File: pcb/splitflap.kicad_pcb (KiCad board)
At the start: 2 copper layers, 96 x 45 mm, 62 parts, among them J1 Motor A, J10 Hall C, J11 Hall-D, J12 Conn_01x03, J13 Conn_01x03, J14 Conn_01x03, J15 Conn_01x03, J2 Motor B, J3 Motor C, J4 Motor D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

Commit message: Make sure mouse bites aren't deleted upon import
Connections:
- J7 pad 1: +5V -> +12V
- J7 pad 3: unconnected-(J7-Pad3) -> GND
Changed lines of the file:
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@@
   (net 63 "Net-(J6-Pin_1)")
   (net 64 "Net-(J6-Pin_3)")
-  (net 65 "unconnected-(J7-Pad3)")
+  (net 65 "+12V")
   (net 66 "Net-(J12-Pin_3)")
   (net 67 "Net-(J12-Pin_2)")
@@
       (stroke (width 0.1) (type solid)) (layer "F.Fab"))
     (pad "1" thru_hole rect (at 0 0 90) (size 4.6 2) (drill oval 3.6 1) (layers "*.Cu" "*.Mask")
-      (net 8 "+5V") (pintype "passive"))
+      (net 65 "+12V") (pintype "passive"))
     (pad "2" thru_hole oval (at 0 6.3 90) (size 4.2 2) (drill oval 3.2 1) (layers "*.Cu" "*.Mask")
       (net 29 "GND") (pintype "passive"))
     (pad "3" thru_hole oval (at 4.8 2.9 90) (size 2 4.2) (drill oval 1 3.2) (layers "*.Cu" "*.Mask")
-      (net 65 "unconnected-(J7-Pad3)") (pintype "passive+no_connect"))
+      (net 29 "GND") (pintype "passive"))
     (model "${KICAD6_3DMODEL_DIR}/Connector_BarrelJack.3dshapes/BarrelJack_GCT_DCJ200-10-A_Horizontal.wrl"
       (offset (xyz 0 0 0))
@@
   (footprint "Panelization:mouse-bite-2mm-slot" (layer "F.Cu")
     (at 166 117.5 90)
-    (attr through_hole)
+    (attr through_hole board_only)
     (fp_text reference "mouse-bite-2mm-slot1" (at 0 -2 90) (layer "F.SilkS") hide
         (effects (font (size 1 1) (thickness 0.2)))
@@
   (footprint "Panelization:mouse-bite-2mm-slot" (layer "F.Cu")
     (at 166 108.5 90)
-    (attr through_hole)
+    (attr through_hole board_only)
     (fp_text reference "mouse-bite-2mm-slot3" (at 0 -2 90) (layer "F.SilkS") hide
         (effects (font (size 1 1) (thickness 0.2)))
@@
   (footprint "Panelization:mouse-bite-2mm-slot" (layer "F.Cu")
     (at 166 126.5 90)
-    (attr through_hole)
+    (attr through_hole board_only)
     (fp_text reference "mouse-bite-2mm-slot" (at 0 -2 90) (layer "F.SilkS") hide
         (effects (font (size 1 1) (thickness 0.2)))
@@
   (footprint "Panelization:mouse-bite-2mm-slot" (layer "F.Cu")
     (at 166 99.5 90)
-    (attr through_hole)
+    (attr through_hole board_only)
     (fp_text reference "mouse-bite-2mm-slot5" (at 0 -2 90) (layer "F.SilkS") hide
         (effects (font (size 1 1) (thickness 0.2)))
@@
   (footprint "Panelization:mouse-bite-2mm-slot" (layer "F.Cu")
     (at 176.5 113 180)
-    (attr through_hole)
+    (attr through_hole board_only)
     (fp_text reference "mouse-bite-2mm-slot2" (at 0 -2) (layer "F.SilkS") hide
         (effects (font (size 1 1) (thickness 0.2)))
@@
   (footprint "Panelization:mouse-bite-2mm-slot" (layer "F.Cu")
     (at 166 90.5 90)
-    (attr through_hole)
+    (attr through_hole board_only)
     (fp_text reference "mouse-bite-2mm-slot7" (at 0 -2 90) (layer "F.SilkS") hide
         (effects (font (size 1 1) (thickness 0.2)))
@@
   (footprint "Panelization:mouse-bite-2mm-slot" (layer "F.Cu")
     (at 176.5 122 180)
-    (attr through_hole)
+    (attr through_hole board_only)
     (fp_text reference "mouse-bite-2mm-slot" (at 0 -2) (layer "F.SilkS") hide
         (effects (font (size 1 1) (thickness 0.2)))
@@
   (footprint "Panelization:mouse-bite-2mm-slot" (layer "F.Cu")
     (at 176.5 104 180)
-    (attr through_hole)
+    (attr through_hole board_only)
     (fp_text reference "mouse-bite-2mm-slot4" (at 0 -2) (layer "F.SilkS") hide
         (effects (font (size 1 1) (thickness 0.2)))
@@
   (footprint "Panelization:mouse-bite-2mm-slot" (layer "F.Cu")
     (at 176.5 95 180)
-    (attr through_hole)
+    (attr through_hole board_only)
     (fp_text reference "mouse-bite-2mm-slot6" (at 0 -2) (layer "F.SilkS") hide
         (effects (font (size 1 1) (thickness 0.2)))

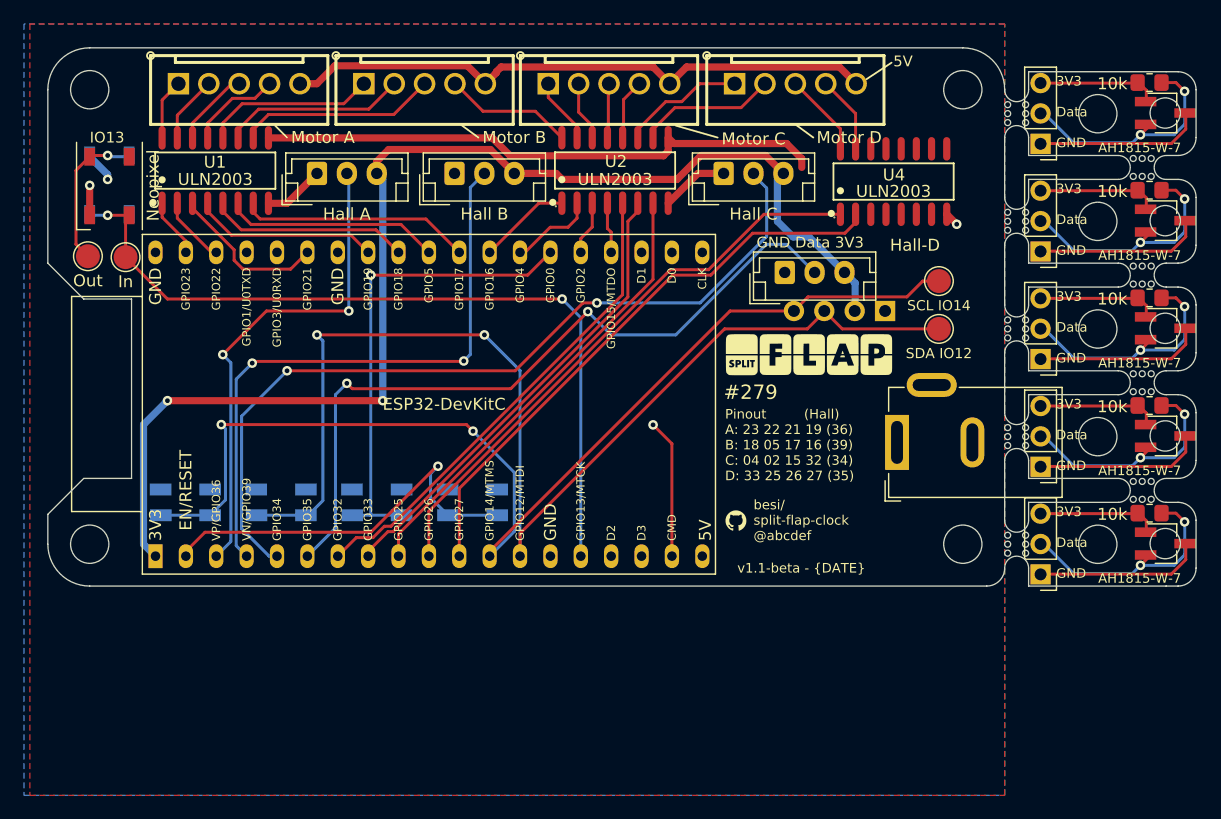
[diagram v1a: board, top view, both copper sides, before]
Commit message: Add 12V-enabled power supply
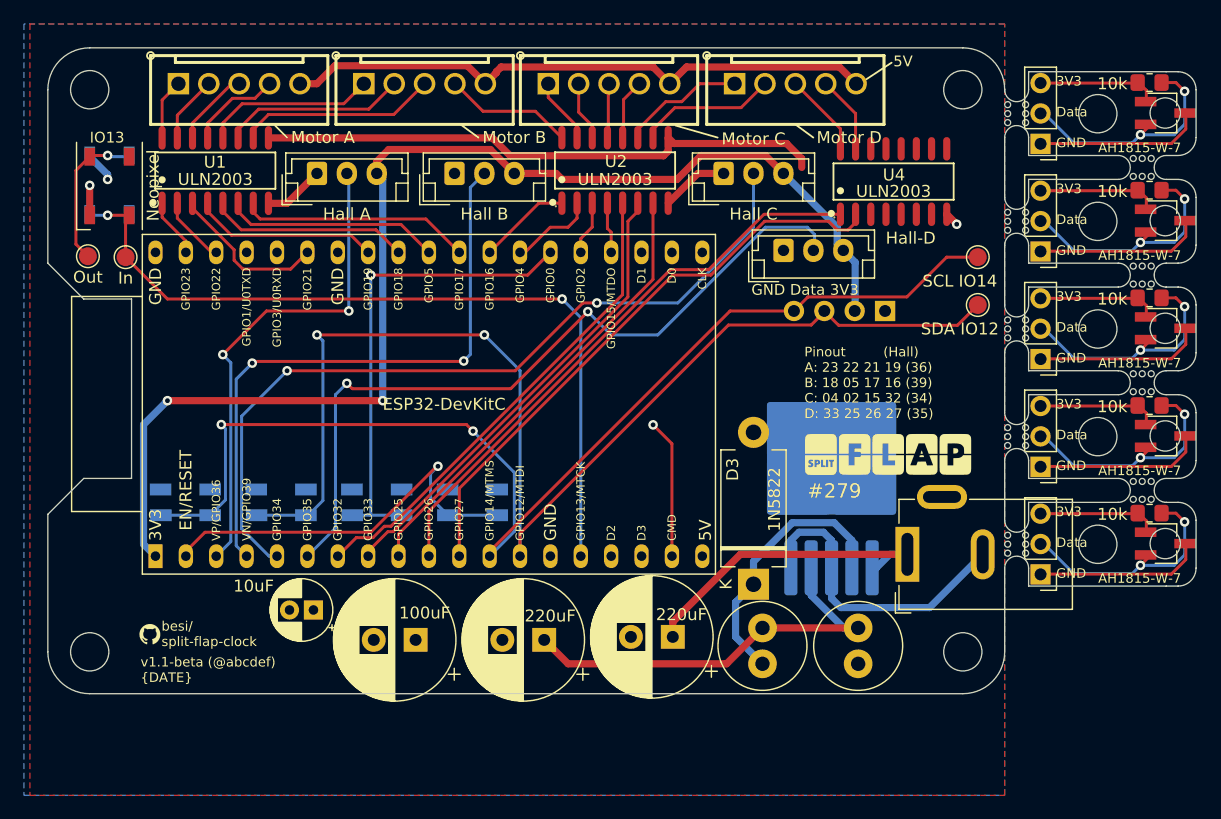
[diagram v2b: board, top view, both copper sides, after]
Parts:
- added C6: 220uF, Capacitor_THT:CP_Radial_D10.0mm_P3.50mm, F.Cu at (137.2, 134.2)
- added C7: 220uF, Capacitor_THT:CP_Radial_D10.0mm_P3.50mm, F.Cu at (126.5, 134.5)
- added C8: 100uF, Capacitor_THT:CP_Radial_D10.0mm_P3.50mm, F.Cu at (115.8, 134.5)
- added C9: 10uF, Capacitor_THT:CP_Radial_D5.0mm_P2.00mm, F.Cu at (107.2, 132.0)
- added D3: 1N5822, Diode_THT:D_DO-201_P12.70mm_Horizontal, F.Cu at (144.0, 129.8)
- added L1: 33uH, Inductor_THT:L_Radial_D7.2mm_P3.00mm_Murata_1700, F.Cu at (144.8, 136.5)
- added L2: 22uH, Inductor_THT:L_Radial_D7.2mm_P3.00mm_Murata_1700, F.Cu at (152.8, 133.5)
- added U12: LM2596S-5, Package_TO_SOT_SMD:TO-263-5_TabPin3, B.Cu at (150.5, 120.8)
- TP1, TP2, TP3, TP4: footprint TestPoint:TestPoint_Pad_D2.0mm -> TestPoint:TestPoint_Pad_D1.5mm
- moved G*** 49.9 mm to (93.5, 134.0)
- moved OSHW1 20.6 mm to (154.2, 95.5)
- moved G*** 18.0 mm to (108.8, 113.2)
- moved G*** 15.5 mm to (133.0, 117.5)
- moved G*** 10.6 mm to (155.2, 119.0)
- moved J7 9.40 mm to (156.9, 127.3)
- moved H2 9.00 mm to (88.5, 135.5)
- moved H4 9.00 mm to (161.5, 135.5)
- moved TP3 3.82 mm to (162.8, 106.5)
- moved TP4 3.82 mm to (162.8, 102.5)
- moved J11 1.84 mm to (146.5, 101.9)
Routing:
- net /POW_FB: track 0.00 -> 35.7 mm
- net +12V: track 0.00 -> 26.6 mm
- net GND: track 14.4 -> 40.3 mm
- net /POW_OUT: track 0.00 -> 22.6 mm
- net GPIO14: track 93.7 -> 97.8 mm
- net GPIO12: track 99.1 -> 103.0 mm
- net GPI34: track 69.2 -> 67.2 mm
- net GPI35: track 62.7 -> 63.9 mm
- net +3V3: track 104.5 -> 103.4 mm
- net GPIO27: track 48.7 -> 49.3 mm
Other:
- board size 96 x 45 mm -> 96 x 54 mm
- board text added: "besi/ split-flap-clock"
- board text added: "v1.1-beta (@abcdef) {DATE}"
- board text removed: "besi/ split-flap-clock @abcdef"
- board text removed: "v1.1-beta - {DATE}"

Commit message: Add qwiic adapter
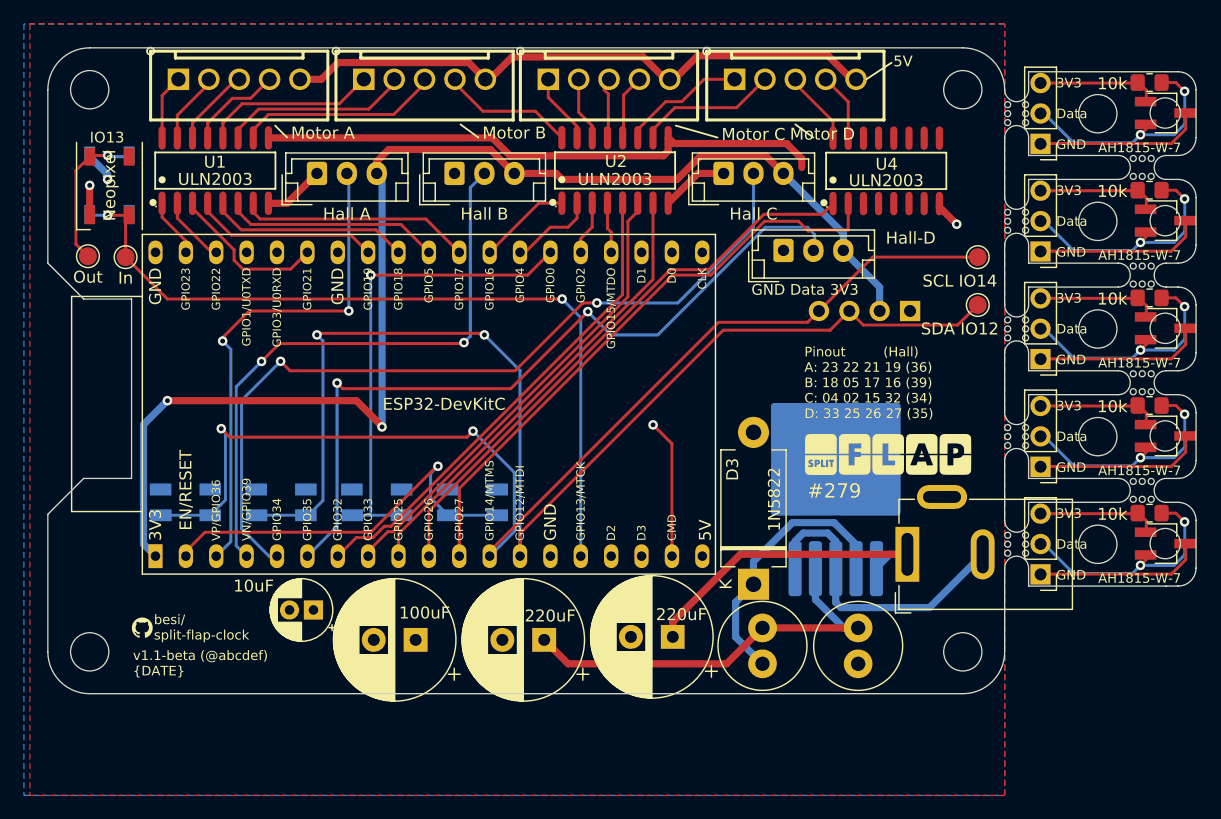
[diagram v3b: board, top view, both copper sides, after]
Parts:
- removed J5: I2C, Connector_PinHeader_2.54mm:PinHeader_1x04_P2.54mm_Vertical
- added U10: ~, qwiic-adapter:qwiic-adapter, B.Cu at (153.3, 107.0)
- moved U4 1.09 mm to (155.1, 95.3)
- moved G*** 0.84 mm to (92.9, 133.5)
- moved J1 0.37 mm to (101.0, 87.6)
- moved J2 0.37 mm to (116.5, 87.6)
- moved J3 0.37 mm to (131.9, 87.6)
- moved J4 0.37 mm to (147.5, 87.6)
- moved U12 0.36 mm to (150.9, 120.9)
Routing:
- net +3V3: track 103.4 -> 107.2 mm
- net GPI34: track 67.2 -> 68.6 mm
- net GPI39: track 51.2 -> 49.9 mm
- net GND: track 40.3 -> 41.3 mm
- net GPI36: track 41.3 -> 42.1 mm
- net Net-(U4-O1): track 7.00 -> 6.22 mm
- net Net-(U4-O2): track 6.48 -> 5.70 mm
- net +5V: track 100.6 -> 101.3 mm
- net GPIO27: track 49.3 -> 50.0 mm
- net GPI35: track 63.9 -> 64.5 mm
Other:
- board text added: "Pinout (Hall) A: 23 22 21 19 (36) B: 18 05 17 16 (39) C: 04 02 15 32 (34) D: 33 25 26 27 (35) Button A / SCL : 14 Button B / SDA : 12"

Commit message: Version 1.1-beta
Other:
- board text added: "v1.1 @f5de51 4. February 2025"
- board text removed: "v1.1-beta (@abcdef) {DATE}"
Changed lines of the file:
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@@
     (effects (font (size 0.9 0.9) (thickness 0.1)) (justify left))
   )
-  (gr_text "v1.1-beta (@abcdef)\n{DATE}\n" (at 92.114438 136.456581) (layer "F.SilkS")
+  (gr_text "v1.1 @f5de51\n4. February 2025" (at 92.114438 136.456581) (layer "F.SilkS")
     (effects (font (size 0.8 0.8) (thickness 0.1)) (justify left))
   )

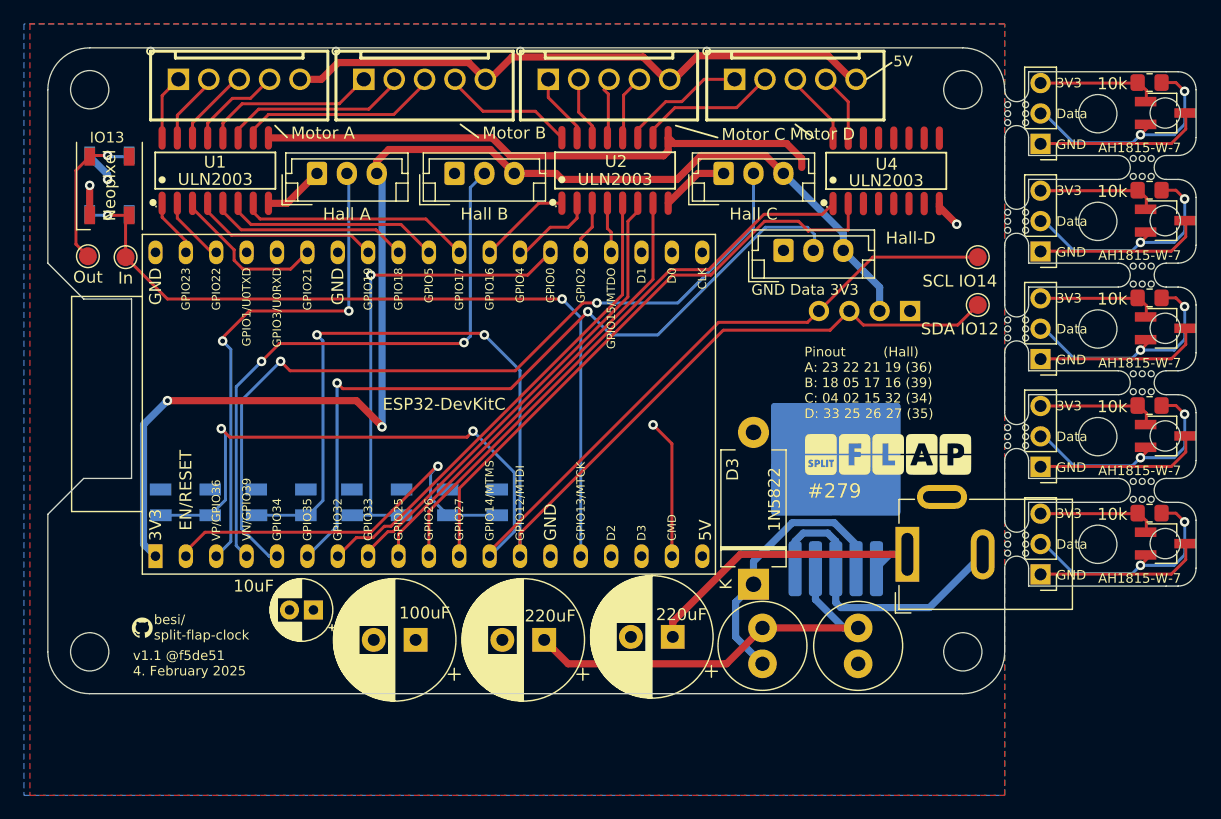
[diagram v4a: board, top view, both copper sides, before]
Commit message: Rework 1
Per EE.SO answer https://electronics.stackexchange.com/a/740530/10810
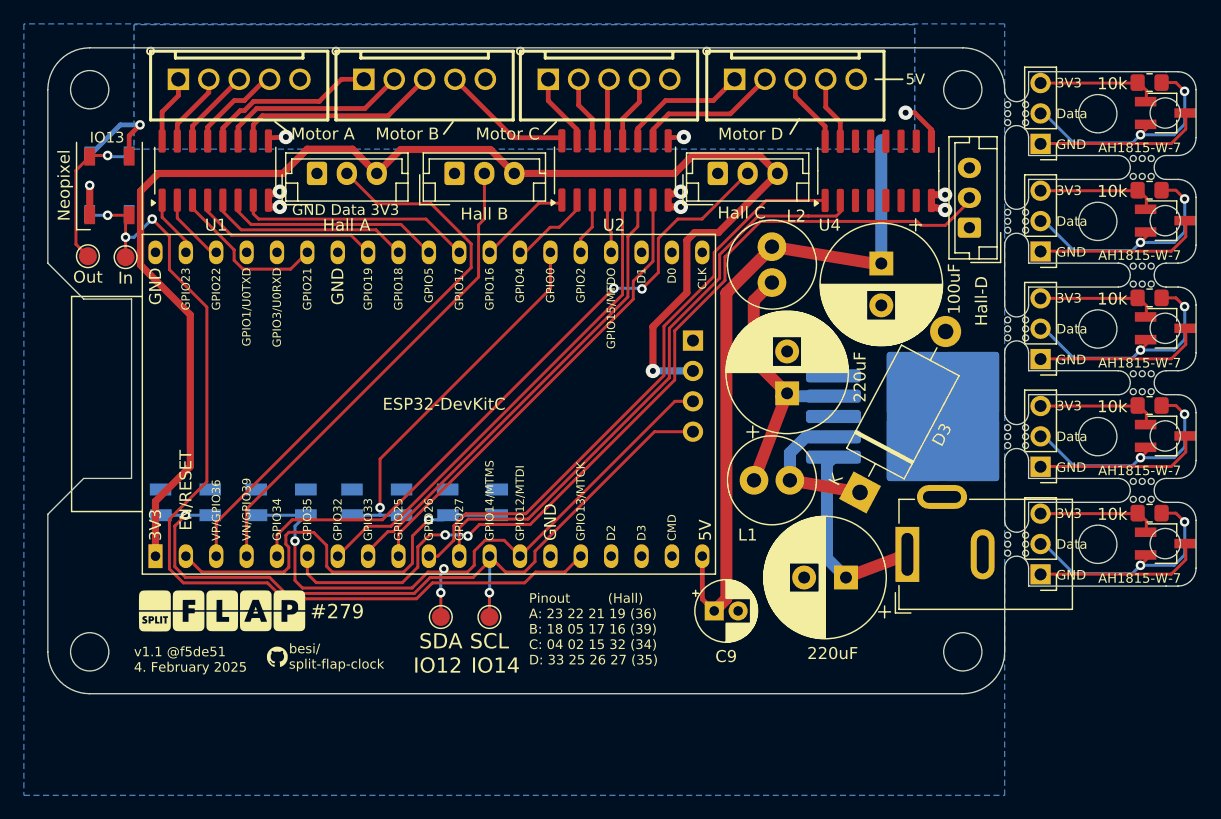
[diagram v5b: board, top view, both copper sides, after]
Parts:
- D3: footprint Diode_THT:D_DO-201_P12.70mm_Horizontal -> Diode_THT:D_DO-201_P15.24mm_Horizontal
- U1, U2, U4: footprint jlc_footprints:SOIC-16_L9.9-W3.9-P1.27-LS6.0-BL -> Package_SO:SOIC-16_3.9x9.9mm_P1.27mm
- moved G*** 57.2 mm to (99.6, 132.1)
- moved TP3 51.9 mm to (117.9, 132.6)
- moved TP4 50.7 mm to (121.9, 132.6)
- moved C8 50.1 mm to (154.7, 103.0), turned to -90 degrees
- moved OSHW1 45.3 mm to (130.6, 134.1)
- moved C9 33.5 mm to (140.7, 132.1), turned to 0 degrees
- moved L2 29.8 mm to (145.5, 104.6), turned to 90 degrees
- moved C7 28.9 mm to (146.8, 113.9), turned to 90 degrees
- moved J11 15.7 mm to (162.1, 100.0), turned to 90 degrees
- moved U10 15.7 mm to (138.9, 113.3), turned to 0 degrees
- moved L1 15.5 mm to (147.0, 121.2), turned to 180 degrees
- moved C6 15.3 mm to (151.7, 129.3)
- moved D3 11.8 mm to (152.9, 122.2), turned to 62 degrees
- moved G*** 11.6 mm to (104.2, 135.9)
- moved G*** 9.11 mm to (125.7, 112.0)
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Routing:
- net GPIO12: track 103.0 -> 56.1 mm, vias 2 -> 3
- net GND: track 41.3 -> 8.43 mm, vias 2 -> 7
- net GPIO14: track 97.7 -> 65.6 mm
- net +5V: track 101.3 -> 73.5 mm, vias 1 -> 4
- net GPI34: track 68.6 -> 55.4 mm
- net /POW_FB: track 35.5 -> 22.8 mm
- net GPIO13: track 67.1 -> 79.2 mm, vias 2 -> 3
- net unconnected-(U3-CMD-Pad18): track 11.6 -> 0.00 mm, vias 1 -> 0
- net GPI35: track 64.5 -> 75.5 mm
- net /POW_OUT: track 22.8 -> 12.4 mm
- net +3V3: track 107.2 -> 117.2 mm, vias 2 -> 1
- net +12V: track 26.3 -> 16.6 mm
- net GPI39: track 49.9 -> 40.2 mm, vias 2 -> 0
- net GPIO0: track 40.0 -> 32.0 mm
- net GPI36: track 42.1 -> 47.8 mm, vias 2 -> 0
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- added copper zone on B.Cu, net +5V
- removed copper zone on F.Cu, net +5V
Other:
- board text added: "GND 3V3 SDA SCL"
- board text removed: "Pinout (Hall) A: 23 22 21 19 (36) B: 18 05 17 16 (39) C: 04 02 15 32 (34) D: 33 25 26 27 (35) Button A / SCL : 14 Button B / SDA : 12"
- board text removed: "SCL SDA 3V3 GND"

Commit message: Rework 2
To be conservative, the traces driving the ULN2003s have been separated out, to prevent capacitive coupling between them. It's "cargo cult engineering", but since we can do it without trouble, how about we do it.
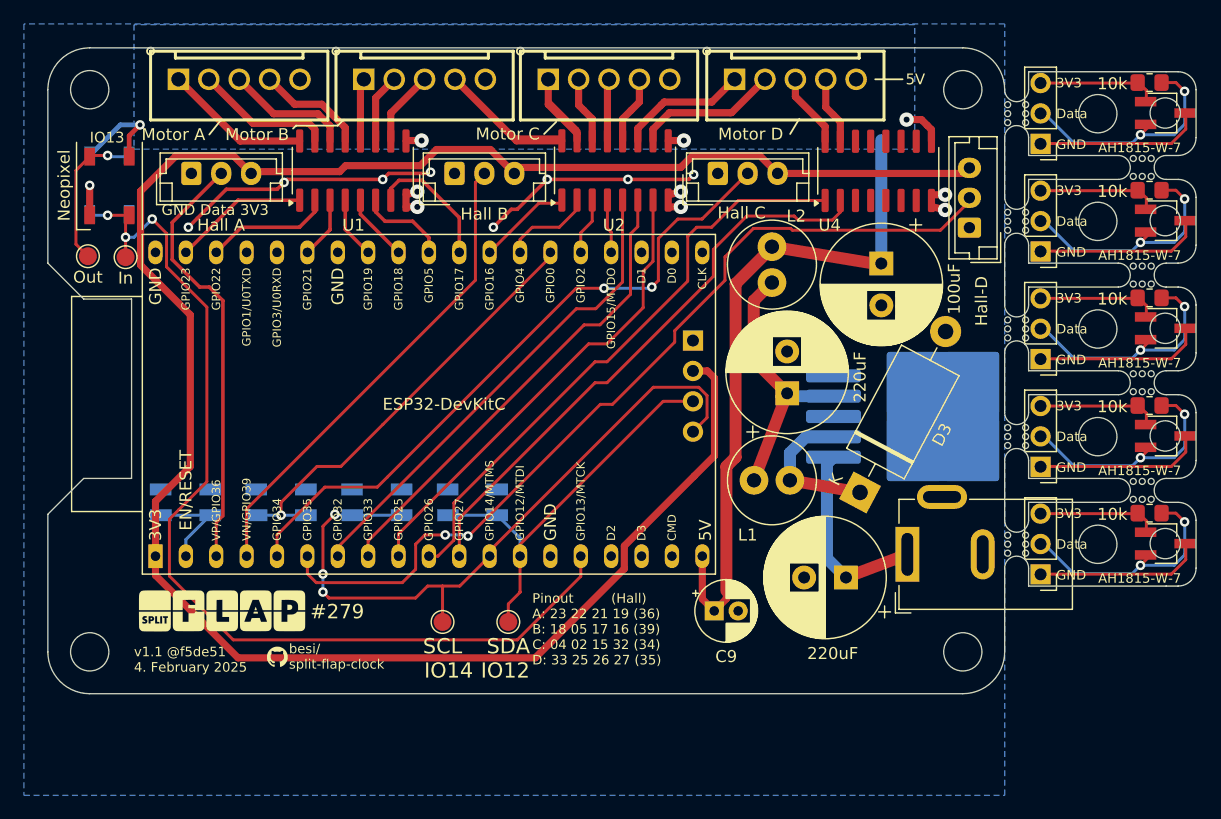
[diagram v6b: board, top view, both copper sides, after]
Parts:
- moved SW4 24.0 mm to (96.5, 123.0)
- moved SW1 16.0 mm to (112.5, 123.0)
- moved SW2 16.0 mm to (120.5, 123.0)
- moved U1 11.5 mm to (110.5, 95.3)
- moved J8 10.5 mm to (97.0, 95.5)
- moved SW3 8.00 mm to (104.5, 123.0)
- moved TP3 5.66 mm to (123.5, 133.0)
- moved TP4 3.94 mm to (118.0, 133.0)
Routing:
- net +3V3: track 117.2 -> 175.5 mm, vias 1 -> 0
- net GND: track 8.43 -> 49.9 mm, vias 7 -> 15
- net RESET: track 35.6 -> 8.39 mm, vias 1 -> 0
- net GPIO12: track 56.1 -> 34.7 mm, vias 3 -> 0
- net Net-(U2-O7): track 11.8 -> 23.9 mm
- net GPI36: track 47.8 -> 36.2 mm
- net GPIO18: track 16.8 -> 5.68 mm
- net Net-(U2-O1): track 11.0 -> 22.0 mm
- net Net-(U1-O7): track 17.3 -> 6.33 mm
- net GPIO5: track 18.1 -> 7.56 mm
- net GPIO19: track 15.5 -> 5.15 mm
- net Net-(U1-O6): track 15.9 -> 5.80 mm
- net Net-(U1-O5): track 15.0 -> 5.28 mm
- net GPIO17: track 20.0 -> 11.2 mm
- net GPIO21: track 13.2 -> 5.15 mm
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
